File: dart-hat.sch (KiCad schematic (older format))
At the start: 24 parts, among them J0 XT60 Female

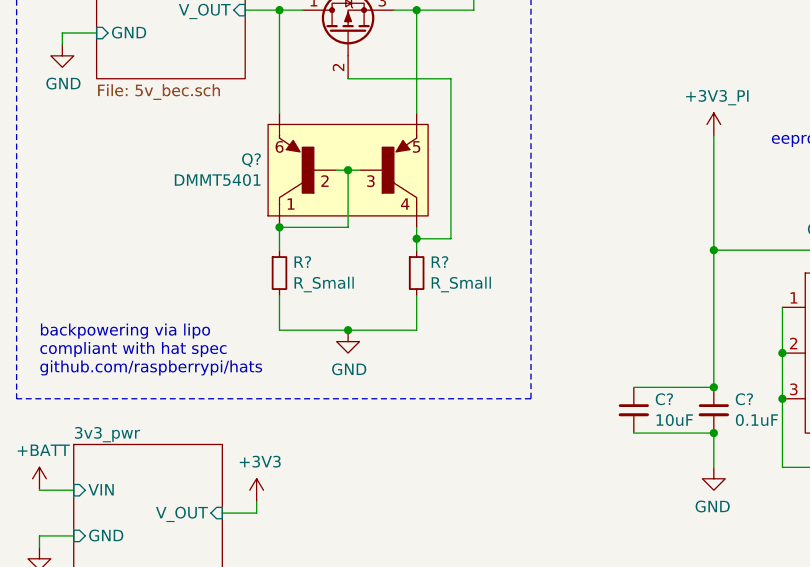
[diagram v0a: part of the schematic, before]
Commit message: [main] update zvd resistor values
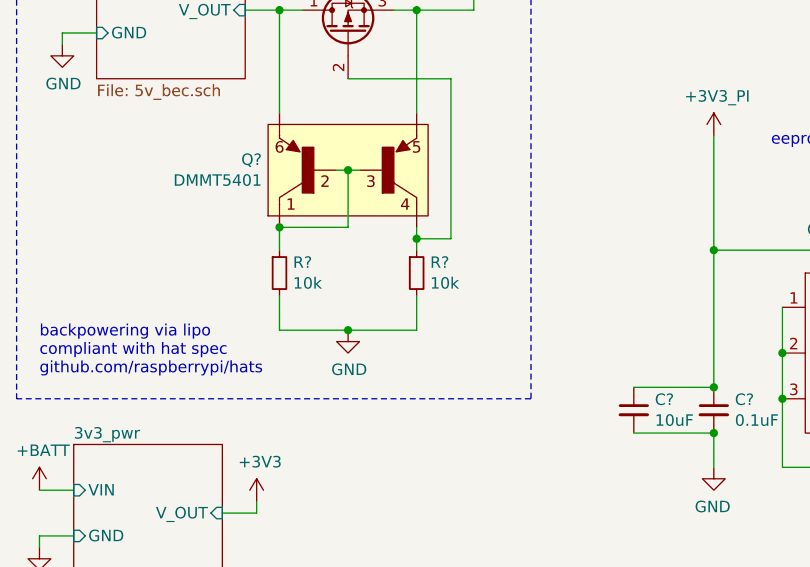
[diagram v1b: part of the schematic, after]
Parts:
- R? (x2): value R_Small -> 10k
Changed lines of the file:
@@
 P 1800 3950
 F 0 "R?" H 1859 3996 50  0000 L CNN
-F 1 "R_Small" H 1859 3905 50  0000 L CNN
+F 1 "10k" H 1859 3905 50  0000 L CNN
 F 2 "" H 1800 3950 50  0001 C CNN
 F 3 "~" H 1800 3950 50  0001 C CNN
@@
 P 2400 3950
 F 0 "R?" H 2459 3996 50  0000 L CNN
-F 1 "R_Small" H 2459 3905 50  0000 L CNN
+F 1 "10k" H 2459 3905 50  0000 L CNN
 F 2 "" H 2400 3950 50  0001 C CNN
 F 3 "~" H 2400 3950 50  0001 C CNN

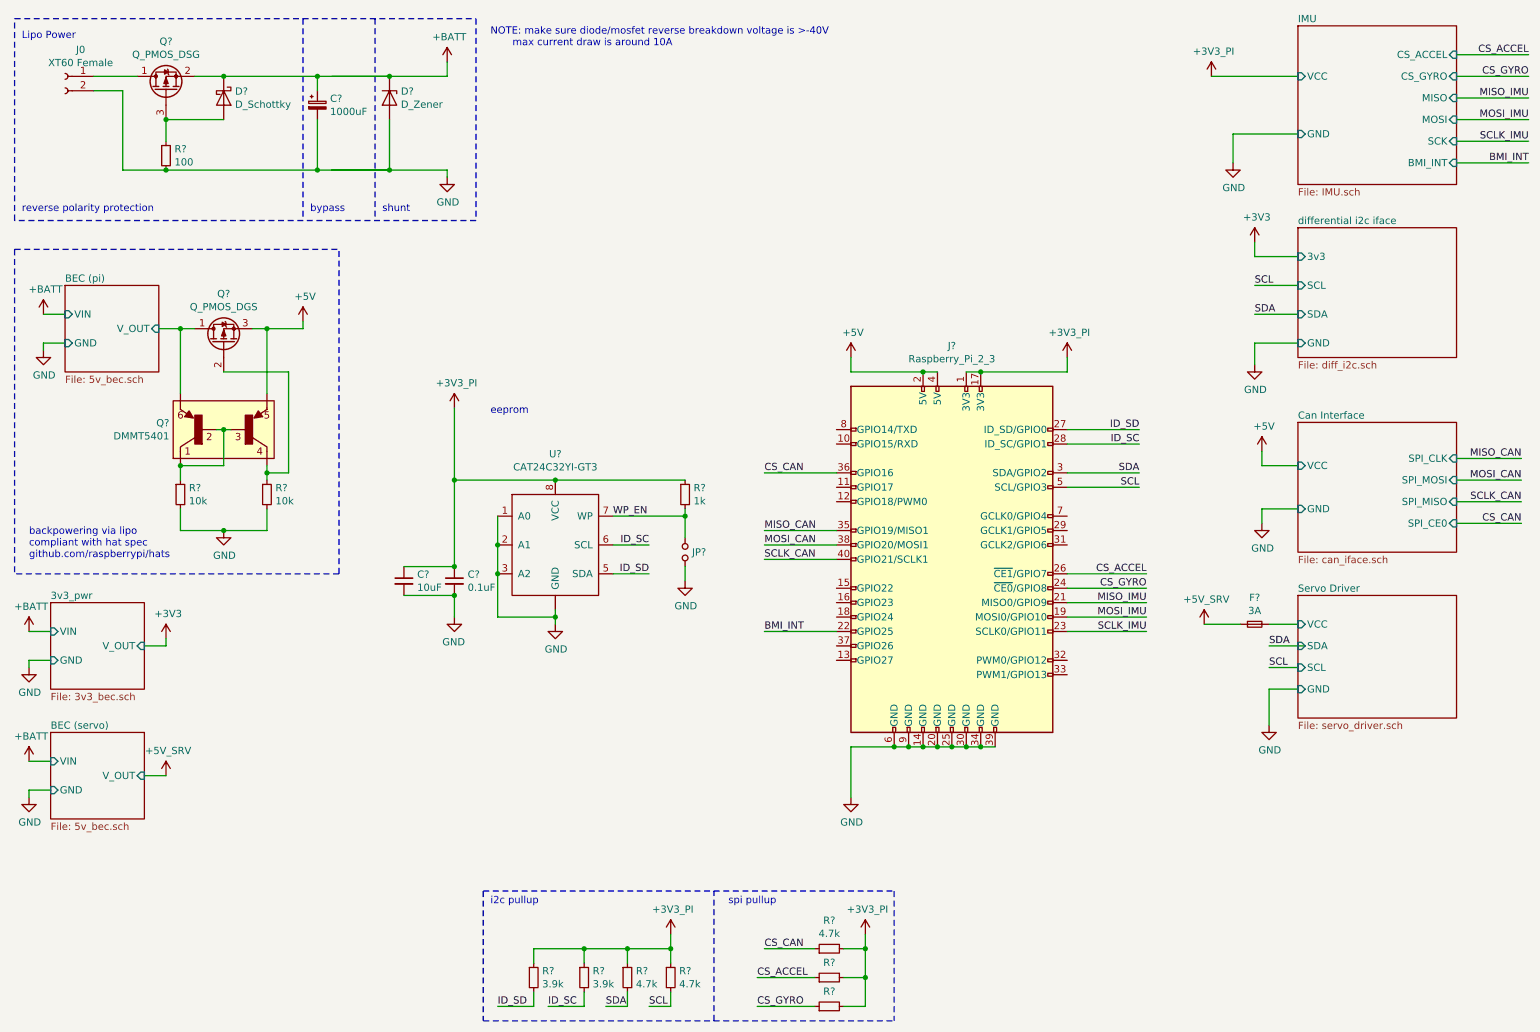
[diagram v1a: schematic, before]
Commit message: update reference ids, assign value to c8
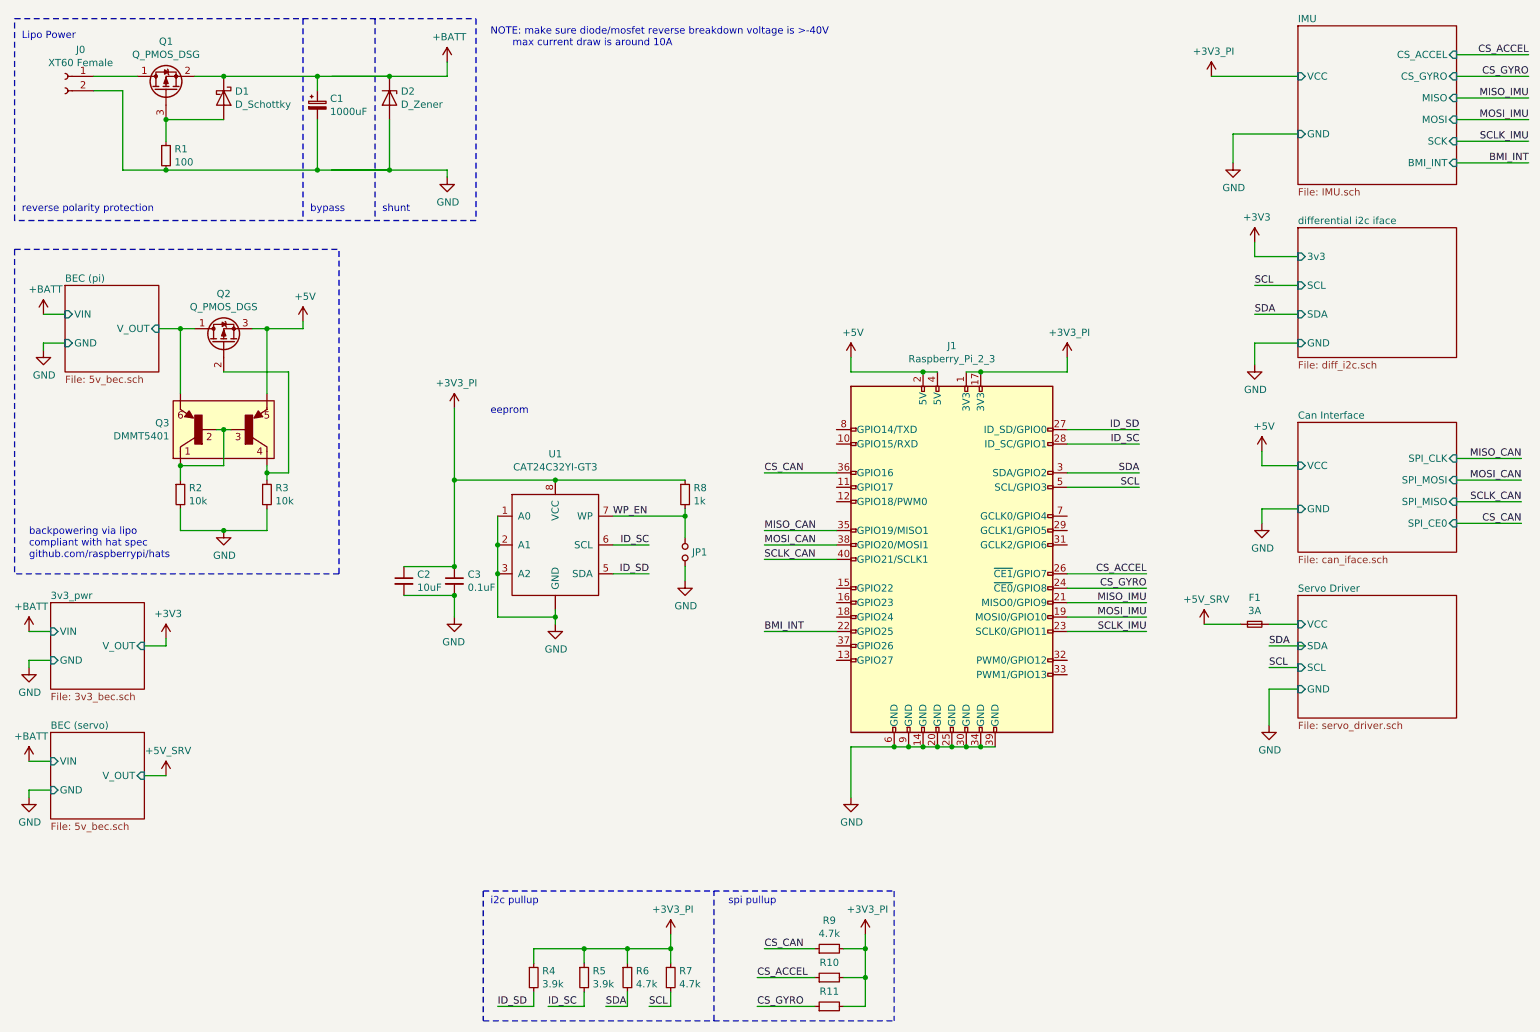
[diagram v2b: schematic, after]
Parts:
- gave numbers to parts that had none: 23

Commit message: no longer a hat lol
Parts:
- removed Q2: Q_PMOS_DGS, symbol Device:Q_PMOS_DGS
- added D8, D9: LED_Small, LED_SMD:LED_0805_2012Metric_Pad1.15x1.40mm_HandSolder, symbol Device:LED_Small
- added Q2: Q_PMOS_DSG, Package_TO_SOT_SMD:TO-263-3_TabPin2, symbol Device:Q_PMOS_DSG
- added R23, R24: 120, Resistor_SMD:R_0805_2012Metric_Pad1.15x1.40mm_HandSolder, symbol Device:R_Small
- added TP0, TP1, TP2, TP3, TP4: TestPoint, TestPoint:TestPoint_Pad_D2.5mm, symbol Connector:TestPoint
- C2, C3: footprint (none) -> Capacitor_SMD:C_0805_2012Metric_Pad1.15x1.40mm_HandSolder
- CP1: renamed from C1; footprint (none) -> EEE-TP1J102M:CAP_EEETP1J102M
- D1: footprint (none) -> Package_TO_SOT_THT:TO-220-2_Horizontal_TabUp
- D2: footprint (none) -> Diode_SMD:D_SOD-523
- F1: footprint (none) -> Fuse:Fuse_0805_2012Metric_Pad1.15x1.40mm_HandSolder
- J0: footprint (none) -> XT60PW-M:AMASS_XT60PW-M
- J1: footprint (none) -> Connector_PinHeader_2.54mm:PinHeader_2x20_P2.54mm_Vertical
- JP1: footprint (none) -> Connector_PinHeader_2.54mm:PinHeader_1x02_P2.54mm_Vertical
- Q1: footprint (none) -> Package_TO_SOT_SMD:TO-263-3_TabPin2
- Q3: footprint SOT95P285X140-6N -> DMMT5401:SOT95P285X140-6N
- R1: value 100 -> 10k; footprint (none) -> Resistor_SMD:R_0805_2012Metric_Pad1.15x1.40mm_HandSolder
- R10, R11, R2, R3, R4, R5, R6, R7, R8, R9: footprint (none) -> Resistor_SMD:R_0805_2012Metric_Pad1.15x1.40mm_HandSolder
- U1: footprint (none) -> CAT24C32YI-GT3:SOP65P640X120-8N
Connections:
- net +5V: now also Q2.2 (S), TP2.1
- net +5V_SRV: now also TP3.1
- net +BATT: now also TP0.1
- net BEC (pi)/V_OUT: now also Q2.1 (D)
- net GND: now also D1.2 (A), R23.1, R24.1; no longer D2.2 (A)
- net CAN_INT: now reaches J1.16 (GPIO23)
- net LED0: now reaches J1.32 (PWM0/GPIO12)
- net LED0: now also D8.2 (A)
- net LED1: now reaches J1.33 (PWM1/GPIO13)
- net LED1: now also D9.2 (A)
- net at Q1.3 (G), R1.1: now also D2.2 (A), TP1.1; no longer D1.2 (A)
- net at Q3.4, R3.1: now also Q2.3 (G)
- net Servo Driver/VCC renamed Servo Driver/5V_IN
- net Servo Driver/5V_IN: now also TP4.1
- new net: D8.1 (K), R23.2
- new net: D9.1 (K), R24.2
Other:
- note added: "GPIO LEDs"
- note removed: "NOTE: make sure diode/mosfet reverse breakdown voltage is >-40V\n max current draw is around 10A"
- moved on the sheet: D1, D2, F1

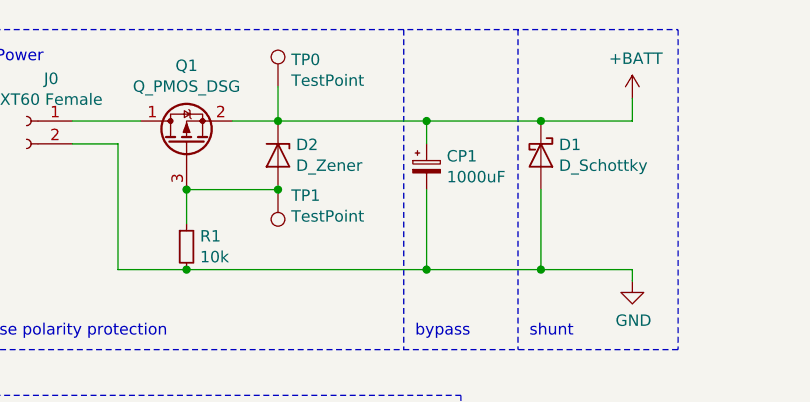
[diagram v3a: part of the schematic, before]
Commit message: [schematic] fix 3v3 symbol pin to use 3v3_pi instead of 5V_SRV
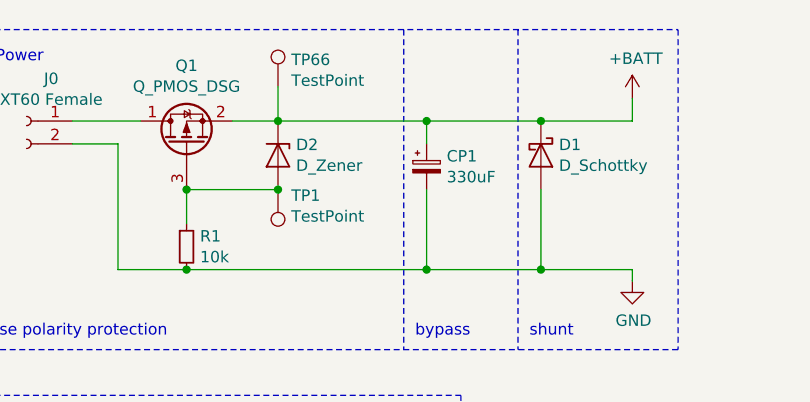
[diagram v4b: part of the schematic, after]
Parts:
- CP1: value 1000uF -> 330uF; footprint EEE-TP1J102M:CAP_EEETP1J102M -> Capacitor_THT:CP_Radial_D10.0mm_P5.00mm
- Q2: footprint Package_TO_SOT_SMD:TO-263-3_TabPin2 -> Package_SO:SOIC-8-1EP_3.9x4.9mm_P1.27mm_EP2.29x3mm
- renumbered TP0 to TP66
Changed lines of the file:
@@
 AR Path="/619F5AAC" Ref="CP1"  Part="1"
 F 0 "CP1" H 2838 1296 50  0000 L CNN
-F 1 "1000uF" H 2838 1205 50  0000 L CNN
-F 2 "EEE-TP1J102M:CAP_EEETP1J102M" H 2750 1250 50  0001 C CNN
+F 1 "330uF" H 2838 1205 50  0000 L CNN
+F 2 "Capacitor_THT:CP_Radial_D10.0mm_P5.00mm" H 2750 1250 50  0001 C CNN
 F 3 "~" H 2750 1250 50  0001 C CNN
 	1    2750 1250
@@
 Wire Wire Line
 	2100 1050 2750 1050
-$Comp
-L Device:Q_PMOS_DSG Q?
-U 1 1 61A72D78
-P 2100 2900
-AR Path="/61AC98FF/61A72D78" Ref="Q?"  Part="1"
-AR Path="/61A72D78" Ref="Q2"  Part="1"
-F 0 "Q2" V 2442 2900 50  0000 C CNN
-F 1 "Q_PMOS_DSG" V 2351 2900 50  0000 C CNN
-F 2 "Package_TO_SOT_SMD:TO-263-3_TabPin2" H 2300 3000 50  0001 C CNN
-F 3 "~" H 2100 2900 50  0001 C CNN
-	1    2100 2900
-	0    -1   -1   0
-$EndComp
 Wire Wire Line
 	7950 3800 8450 3800
@@
 Connection ~ 2100 1350
 $Comp
-L Connector:TestPoint TP0
+L Connector:TestPoint TP66
 U 1 1 61B5F8F9
 P 2100 900
-F 0 "TP0" H 2042 1018 50  0000 R CNN
+F 0 "TP66" H 2042 1018 50  0000 R CNN
 F 1 "TestPoint" H 2042 927 50  0000 R CNN
 F 2 "TestPoint:TestPoint_Pad_D2.5mm" H 2300 900 50  0001 C CNN
@@
 	1    0    0    -1
 $EndComp
+$Comp
+L Device:Q_PMOS_DSG Q?
+U 1 1 61A72D78
+P 2100 2900
+AR Path="/61AC98FF/61A72D78" Ref="Q?"  Part="1"
+AR Path="/61A72D78" Ref="Q2"  Part="1"
+F 0 "Q2" V 2442 2900 50  0000 C CNN
+F 1 "Q_PMOS_DSG" V 2351 2900 50  0000 C CNN
+F 2 "Package_SO:SOIC-8-1EP_3.9x4.9mm_P1.27mm_EP2.29x3mm" H 2300 3000 50  0001 C CNN
+F 3 "~" H 2100 2900 50  0001 C CNN
+	1    2100 2900
+	0    -1   -1   0
+$EndComp
 $EndSCHEMATC

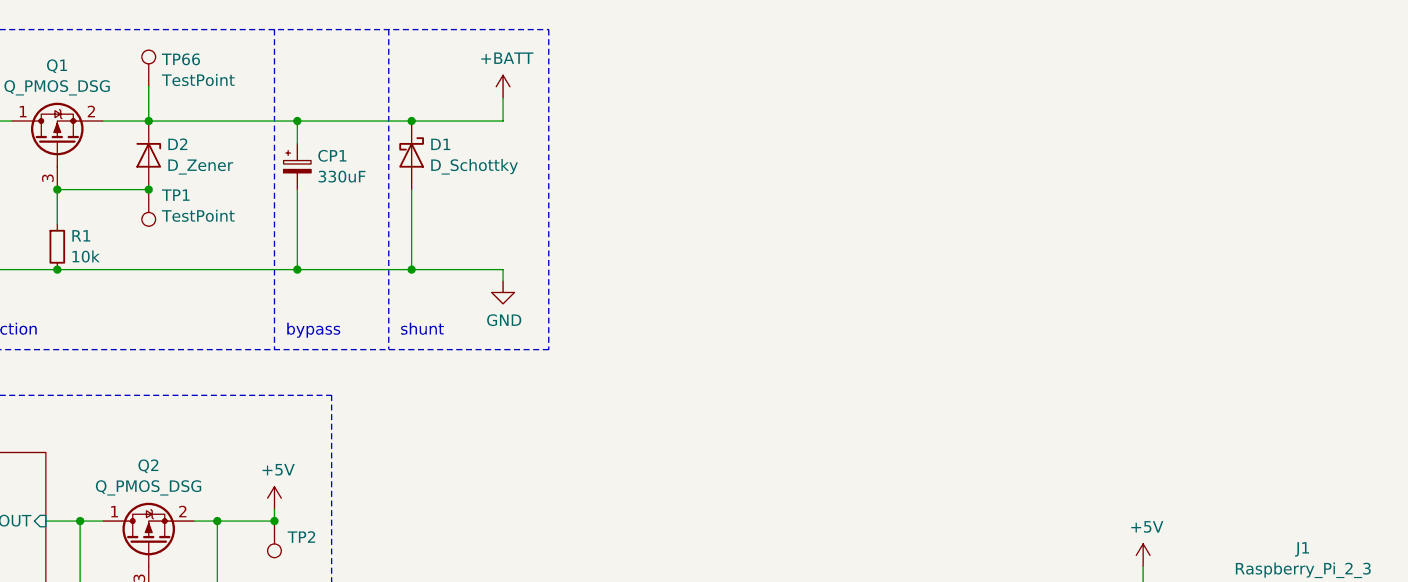
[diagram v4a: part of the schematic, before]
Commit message: [power supply] basic schematic for new 5V power supply, LM25088MH-2
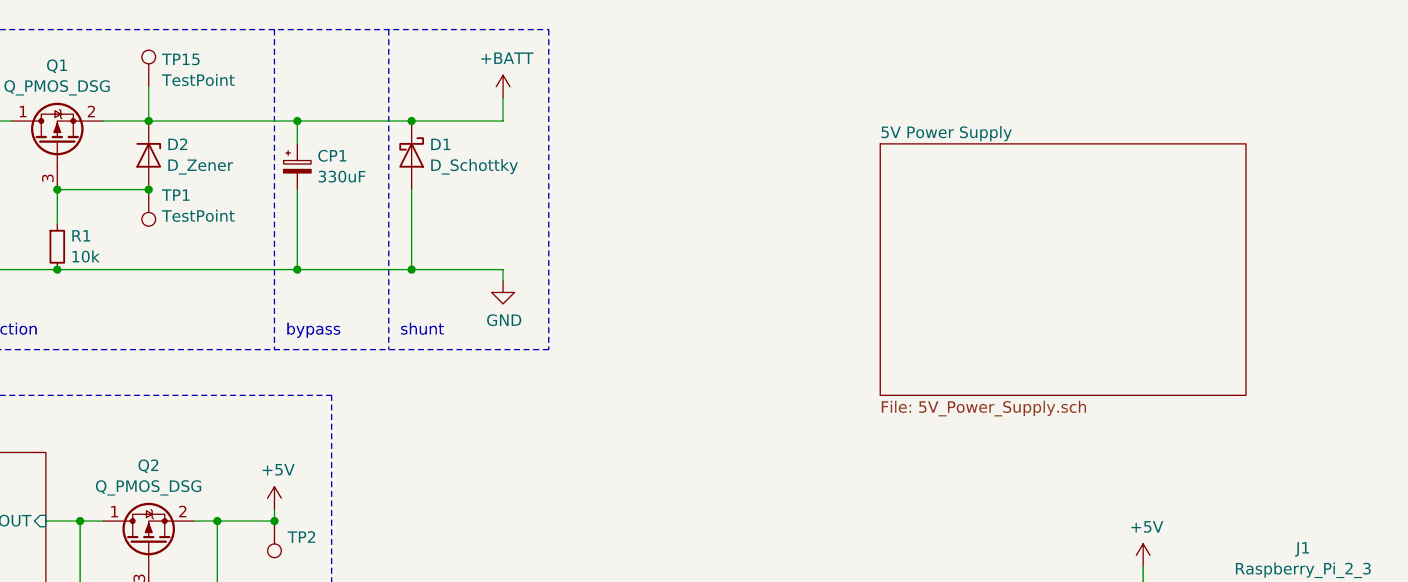
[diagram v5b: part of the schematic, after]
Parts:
- TP1, TP2, TP3, TP4: footprint TestPoint:TestPoint_Pad_D2.5mm -> TestPoint:TestPoint_Pad_D1.0mm
- TP15: renamed from TP66; footprint TestPoint:TestPoint_Pad_D2.5mm -> TestPoint:TestPoint_Pad_D1.0mm
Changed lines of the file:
@@
 $Descr A4 11693 8268
 encoding utf-8
-Sheet 1 8
+Sheet 1 9
 Title ""
 Date ""
@@
 F 0 "TP1" H 2042 1376 50  0000 R CNN
 F 1 "TestPoint" H 2042 1467 50  0000 R CNN
-F 2 "TestPoint:TestPoint_Pad_D2.5mm" H 2300 1350 50  0001 C CNN
+F 2 "TestPoint:TestPoint_Pad_D1.0mm" H 2300 1350 50  0001 C CNN
 F 3 "~" H 2300 1350 50  0001 C CNN
 	1    2100 1350
@@
 Connection ~ 2100 1350
 $Comp
-L Connector:TestPoint TP66
+L Connector:TestPoint TP15
 U 1 1 61B5F8F9
 P 2100 900
-F 0 "TP66" H 2042 1018 50  0000 R CNN
+F 0 "TP15" H 2042 1018 50  0000 R CNN
 F 1 "TestPoint" H 2042 927 50  0000 R CNN
-F 2 "TestPoint:TestPoint_Pad_D2.5mm" H 2300 900 50  0001 C CNN
+F 2 "TestPoint:TestPoint_Pad_D1.0mm" H 2300 900 50  0001 C CNN
 F 3 "~" H 2300 900 50  0001 C CNN
 	1    2100 900
@@
 F 0 "TP2" H 2592 2872 50  0000 R CNN
 F 1 "TestPoint" H 2592 2917 50  0001 R CNN
-F 2 "TestPoint:TestPoint_Pad_D2.5mm" H 2850 2800 50  0001 C CNN
+F 2 "TestPoint:TestPoint_Pad_D1.0mm" H 2850 2800 50  0001 C CNN
 F 3 "~" H 2850 2800 50  0001 C CNN
 	1    2650 2800
@@
 F 0 "TP3" H 8842 5072 50  0000 R CNN
 F 1 "TestPoint" H 8842 5117 50  0001 R CNN
-F 2 "TestPoint:TestPoint_Pad_D2.5mm" H 9100 5000 50  0001 C CNN
+F 2 "TestPoint:TestPoint_Pad_D1.0mm" H 9100 5000 50  0001 C CNN
 F 3 "~" H 9100 5000 50  0001 C CNN
 	1    8900 5000
@@
 F 0 "TP4" H 9358 4972 50  0000 L CNN
 F 1 "TestPoint" H 9358 4927 50  0001 L CNN
-F 2 "TestPoint:TestPoint_Pad_D2.5mm" H 9500 4900 50  0001 C CNN
+F 2 "TestPoint:TestPoint_Pad_D1.0mm" H 9500 4900 50  0001 C CNN
 F 3 "~" H 9500 4900 50  0001 C CNN
 	1    9300 4900
@@
 	0    -1   -1   0
 $EndComp
+$Sheet
+S 5300 1150 1600 1100
+U 61BC5F5B
+F0 "5V Power Supply" 50
+F1 "5V_Power_Supply.sch" 50
+$EndSheet
 $EndSCHEMATC
